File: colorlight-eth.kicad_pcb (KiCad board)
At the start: 2 copper layers, 27.4 x 46.5 mm, 8 parts, among them J1 Conn_02x15_Odd_Even, J2 2250013-4, J4 Conn_01x05_Male, J5 2250013-4

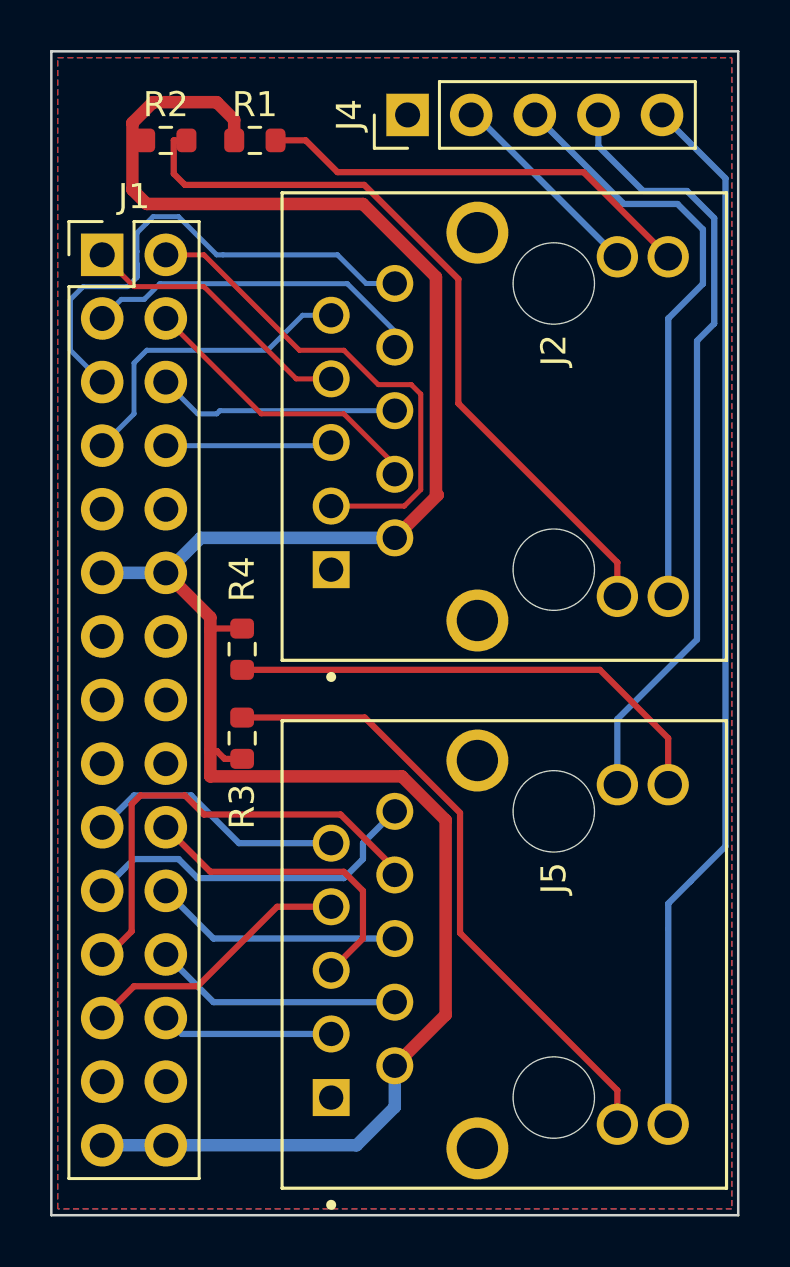
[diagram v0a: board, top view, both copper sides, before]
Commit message: v 1.1 : resistors on the back
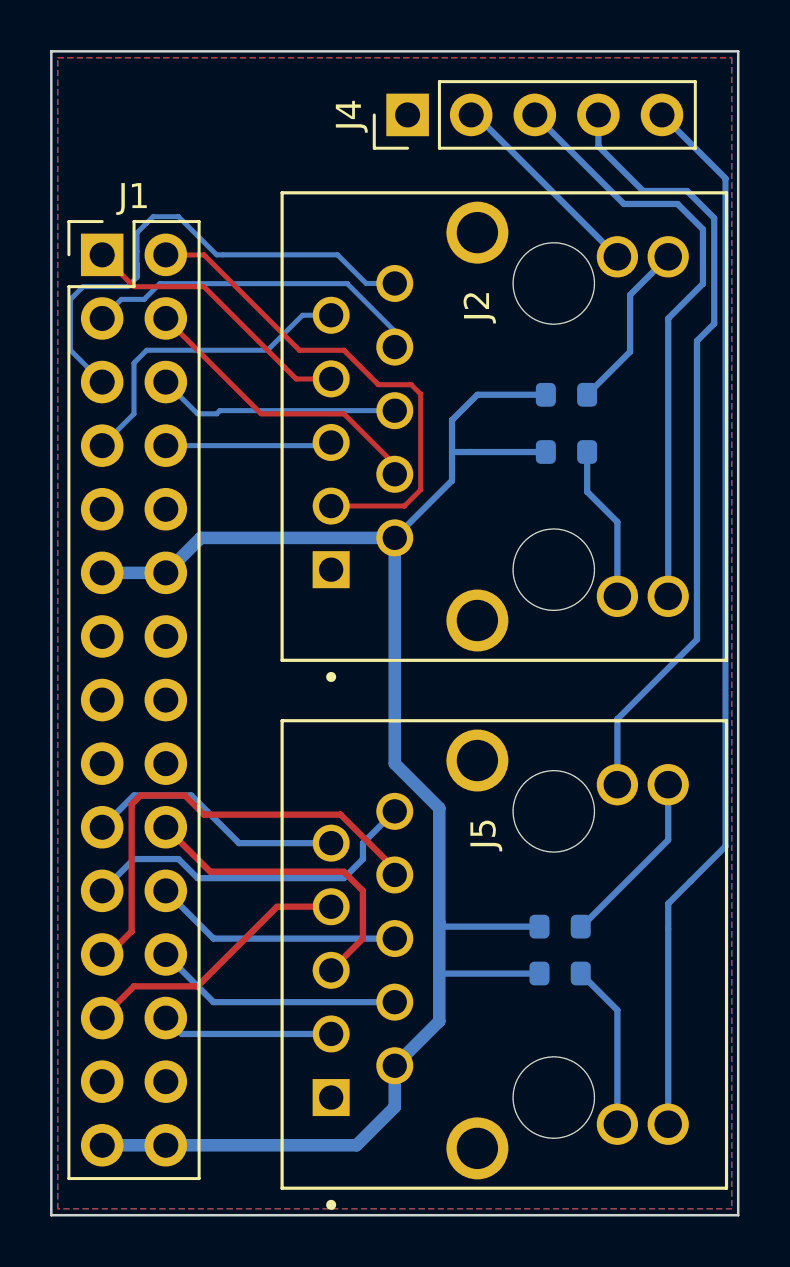
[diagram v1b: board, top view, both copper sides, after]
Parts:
- R1, R2, R3, R4: moved to B.Cu
- moved R2 20.3 mm to (93.7, 79.2)
- moved R4 16.9 mm to (93.5, 98.2), turned to 0 degrees
- moved R1 16.1 mm to (93.7, 77.0)
- moved R3 15.8 mm to (93.5, 100.1), turned to 0 degrees
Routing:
- net Net-(J2-Pad11): track 29.9 -> 6.26 mm
- net 3V3: track 91.5 -> 70.4 mm
- net Net-(J5-Pad11): track 25.3 -> 6.62 mm
- net Net-(J5-Pad14): track 20.0 -> 7.13 mm
- net Net-(J2-Pad14): track 17.6 -> 6.85 mm
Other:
- board text added: "Dual Ethernet PMOD v 1.1 (C) Dave Berkeley 2024"
- board text removed: "Dual Ethernet PMOD v 1.0 (C) Dave Berkeley 2024"

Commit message: v1.2 : fix 5V feed to magnetics
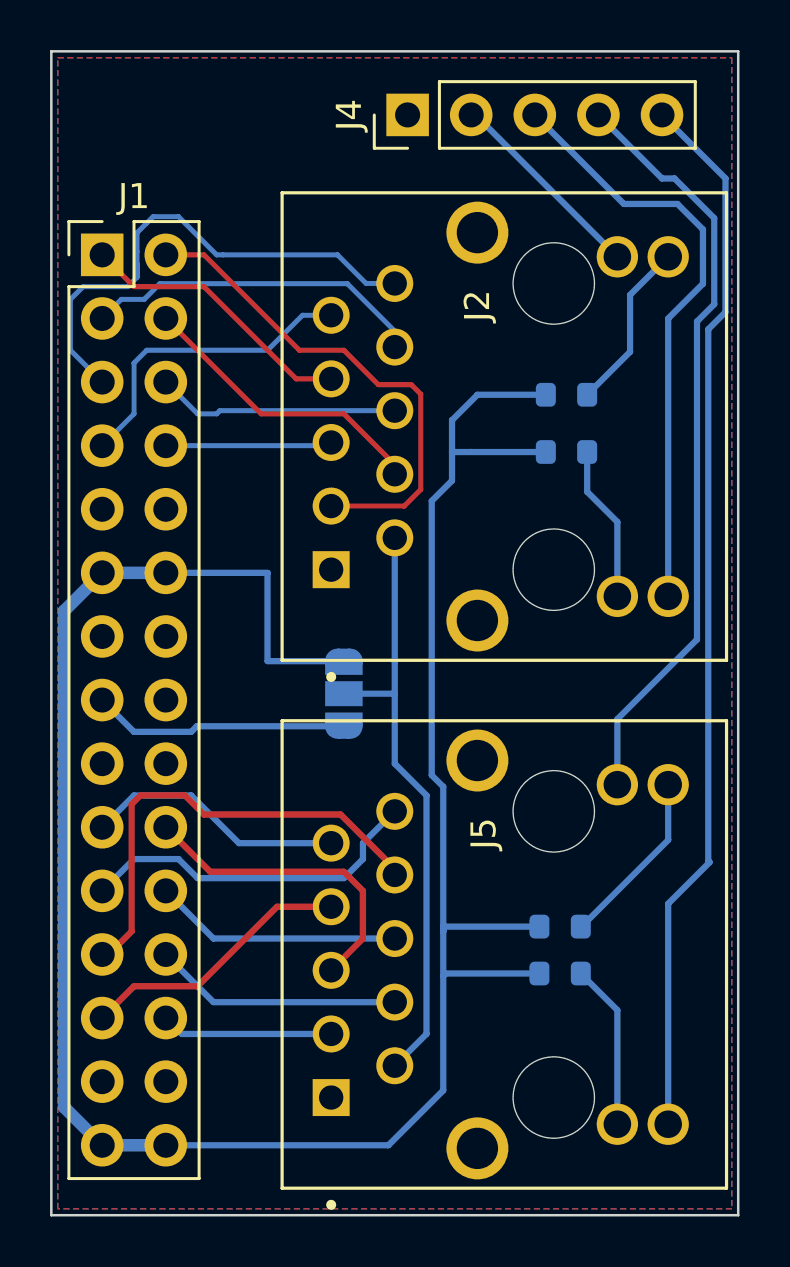
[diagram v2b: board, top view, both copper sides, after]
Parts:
- added JP1: SolderJumper_3_Open, Jumper:SolderJumper-3_P1.3mm_Open_RoundedPad1.0x1.5mm, B.Cu at (84.8, 88.9)
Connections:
- J1 pad 15: 0V -> 5V
- J2 pad 2: 3V3 -> Vcc
- J5 pad 2: 3V3 -> Vcc
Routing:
- net 3V3: track 70.4 -> 95.0 mm
- net Vcc: track 0.00 -> 24.2 mm
- net 5V: track 0.00 -> 10.3 mm
- net LED2_1: track 31.3 -> 30.6 mm
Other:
- board text added: "(C) Dave Berkeley 2024"
- board text added: "3V3"
- board text added: "5V"
- board text added: "Dual Ethernet PMOD v 1.2"
- board text removed: "Dual Ethernet PMOD v 1.1 (C) Dave Berkeley 2024"

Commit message: v 1.3 : mirrored connector pins
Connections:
- J1 pad 1: ETH1_2P -> ETH1_4P
- J1 pad 15: 5V -> 0V
- J1 pad 16: 0V -> 5V
- J1 pad 19: ETH2_1P -> ETH2_3P
- J1 pad 2: ETH1_4P -> ETH1_2P
- J1 pad 20: ETH2_3P -> ETH2_1P
- J1 pad 21: ETH2_1N -> ETH2_3N
- J1 pad 22: ETH2_3N -> ETH2_1N
- J1 pad 23: ETH2_2N -> ETH2_4N
- J1 pad 24: ETH2_4N -> ETH2_2N
- J1 pad 25: ETH2_2P -> ETH2_4P
- J1 pad 26: ETH2_4P -> ETH2_2P
- J1 pad 3: ETH1_2N -> ETH1_4N
- J1 pad 4: ETH1_4N -> ETH1_2N
- J1 pad 5: ETH1_1N -> ETH1_3N
- J1 pad 6: ETH1_3N -> ETH1_1N
- J1 pad 7: ETH1_1P -> ETH1_3P
- J1 pad 8: ETH1_3P -> ETH1_1P
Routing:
- net 0V: track 0.00 -> 8.59 mm
- net ETH2_2N: track 18.8 -> 10.5 mm
- net ETH1_3P: track 6.66 -> 13.4 mm
- net ETH2_4P: track 6.87 -> 13.1 mm
- net ETH1_3N: track 9.72 -> 15.4 mm
- net ETH1_1N: track 20.8 -> 15.2 mm
- net ETH2_3N: track 9.93 -> 15.1 mm
- net ETH2_4N: track 9.93 -> 15.1 mm
- net ETH1_1P: track 12.5 -> 8.76 mm
- net ETH2_1P: track 10.5 -> 6.87 mm
- net ETH1_4P: track 20.1 -> 23.2 mm
- net 5V: track 10.3 -> 7.55 mm
- net ETH1_2P: track 11.2 -> 8.66 mm
- net ETH1_4N: track 11.9 -> 14.5 mm
- net ETH1_2N: track 13.7 -> 11.7 mm
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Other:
- board text added: "Dual Ethernet PMOD v 1.3"
- board text removed: "Dual Ethernet PMOD v 1.2"
